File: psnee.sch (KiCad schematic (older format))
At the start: 3 parts, among them IC1 ATTINY45, P1 CONN_ICSP

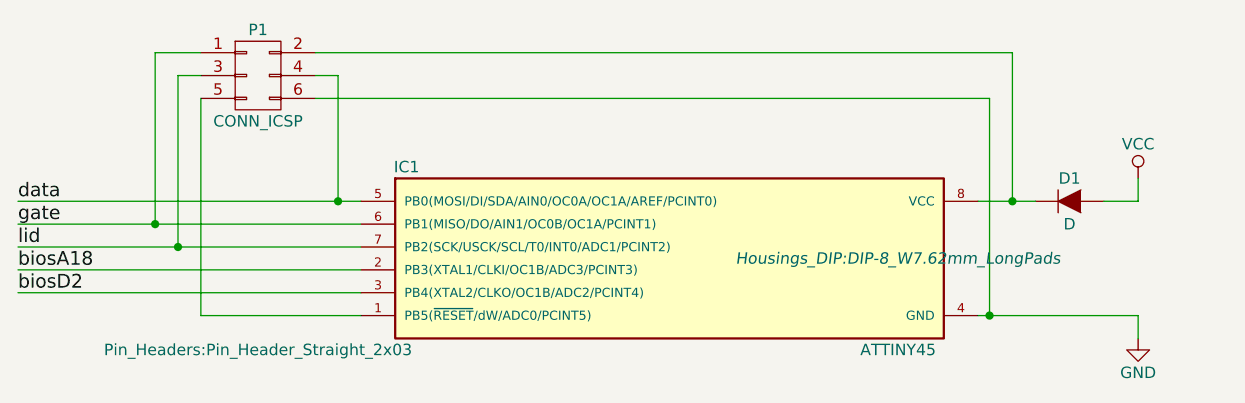
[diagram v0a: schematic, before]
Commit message: updated schematic for v2.0
- added decoupling capacitors
- regenerated annotations
- associated footprints to components
- regenerated netlist
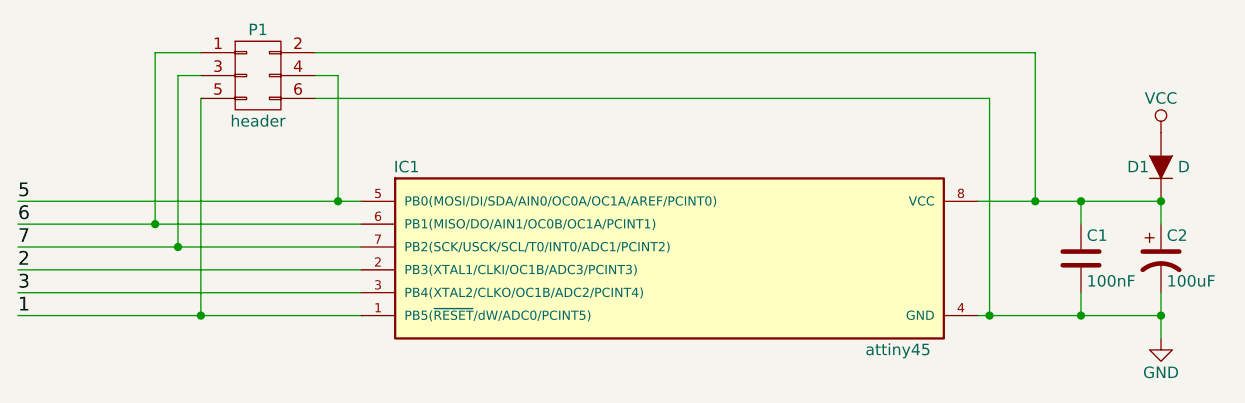
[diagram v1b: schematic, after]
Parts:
- added C1: 100nF, Capacitors_ThroughHole:C_Disc_D6_P5, symbol C
- added C2: 100uF, Capacitors_ThroughHole:C_Radial_D5_L11_P2, symbol CP1
- IC1: value ATTINY45 -> attiny45
- P1: value CONN_ICSP -> header
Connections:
- net GND: now also C1.2, C2.2
- net 1: now reaches IC1.1 (PB5(~RESET~/dW/ADC0/PCINT5)), P1.5 (P5)
- net at D1.1 (K), IC1.8 (VCC), P1.2 (P2): now also C1.1, C2.1
- net biosA18 renamed 2
- net biosD2 renamed 3
- net data renamed 5
- net gate renamed 6
- net lid renamed 7
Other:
- moved on the sheet: D1
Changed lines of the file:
@@
 Sheet 1 1
 Title "PSNee[t]"
-Date "2017-11-02"
-Rev "1.0"
+Date "2018-01-06"
+Rev "2.0"
 Comp ""
 Comment1 ""
@@
 L GND #PWR01
 U 1 1 59F4F857
-P 8050 4000
-F 0 "#PWR01" H 8050 3750 50  0001 C CNN
-F 1 "GND" H 8050 3850 50  0000 C CNN
-F 2 "" H 8050 4000 50  0000 C CNN
-F 3 "" H 8050 4000 50  0000 C CNN
-	1    8050 4000
+P 8150 4000
+F 0 "#PWR01" H 8150 3750 50  0001 C CNN
+F 1 "GND" H 8150 3850 50  0000 C CNN
+F 2 "" H 8150 4000 50  0000 C CNN
+F 3 "" H 8150 4000 50  0000 C CNN
+	1    8150 4000
 	1    0    0    -1
 $EndComp
@@
 P 4200 2850
 F 0 "P1" H 4200 3050 50  0000 C CNN
-F 1 "CONN_ICSP" H 4200 2650 50  0000 C CNN
-F 2 "Pin_Headers:Pin_Header_Straight_2x03" H 4200 1650 50  0000 C CNN
+F 1 "header" H 4200 2650 50  0000 C CNN
+F 2 "Pin_Headers:Pin_Header_Straight_2x03" H 5000 3050 50  0001 C CNN
 F 3 "" H 4200 1650 50  0000 C CNN
 	1    4200 2850
@@
 L D D1
 U 1 1 59F51343
-P 7750 3400
-F 0 "D1" H 7750 3500 50  0000 C CNN
-F 1 "D" H 7750 3300 50  0000 C CNN
-F 2 "Diodes_ThroughHole:Diode_DO-35_SOD27_Horizontal_RM10" H 7750 3400 50  0001 C CNN
-F 3 "" H 7750 3400 50  0000 C CNN
-	1    7750 3400
-	1    0    0    -1
+P 8150 3250
+F 0 "D1" V 8150 3350 50  0000 C CNN
+F 1 "D" V 8150 3150 50  0000 C CNN
+F 2 "Diodes_ThroughHole:Diode_DO-35_SOD27_Horizontal_RM10" H 8150 3250 50  0001 C CNN
+F 3 "" H 8150 3250 50  0000 C CNN
+	1    8150 3250
+	0    -1   -1   0
 $EndComp
 $Comp
 L VCC #PWR02
 U 1 1 59F5217C
-P 8050 3300
-F 0 "#PWR02" H 8050 3150 50  0001 C CNN
-F 1 "VCC" H 8050 3450 50  0000 C CNN
-F 2 "" H 8050 3300 50  0000 C CNN
-F 3 "" H 8050 3300 50  0000 C CNN
-	1    8050 3300
+P 8150 3100
+F 0 "#PWR02" H 8150 2950 50  0001 C CNN
+F 1 "VCC" H 8150 3250 50  0000 C CNN
+F 2 "" H 8150 3100 50  0000 C CNN
+F 3 "" H 8150 3100 50  0000 C CNN
+	1    8150 3100
 	1    0    0    -1
 $EndComp
@@
 P 6000 3650
 F 0 "IC1" H 4850 4050 50  0000 C CNN
-F 1 "ATTINY45" H 7000 3250 50  0000 C CNN
-F 2 "Housings_DIP:DIP-8_W7.62mm_LongPads" H 7000 3650 50  0000 C CIN
+F 1 "attiny45" H 7000 3250 50  0000 C CNN
+F 2 "Housings_DIP:DIP-8_W7.62mm_LongPads" H 6450 4050 50  0001 C CIN
 F 3 "" H 6000 3650 50  0000 C CNN
 	1    6000 3650
 	1    0    0    -1
 $EndComp
-Wire Wire Line
-	7350 3400 7600 3400
-Wire Wire Line
-	7350 3900 8050 3900
+Text Label 3150 3400 0    60   ~ 0
+5
+Text Label 3150 3500 0    60   ~ 0
+6
+Text Label 3150 3600 0    60   ~ 0
+7
+Text Label 3150 3700 0    60   ~ 0
+2
+Text Label 3150 3800 0    60   ~ 0
+3
+Text Label 3150 3900 0    60   ~ 0
+1
+$Comp
+L C C1
+U 1 1 5A5142A1
+P 7800 3650
+F 0 "C1" H 7825 3750 50  0000 L CNN
+F 1 "100nF" H 7825 3550 50  0000 L CNN
+F 2 "Capacitors_ThroughHole:C_Disc_D6_P5" H 7838 3500 50  0001 C CNN
+F 3 "" H 7800 3650 50  0000 C CNN
+	1    7800 3650
+	1    0    0    -1
+$EndComp
+$Comp
+L CP1 C2
+U 1 1 5A5143A7
+P 8150 3650
+F 0 "C2" H 8175 3750 50  0000 L CNN
+F 1 "100uF" H 8175 3550 50  0000 L CNN
+F 2 "Capacitors_ThroughHole:C_Radial_D5_L11_P2" H 8150 3650 50  0001 C CNN
+F 3 "" H 8150 3650 50  0000 C CNN
+	1    8150 3650
+	1    0    0    -1
+$EndComp
 Wire Wire Line
 	3150 3500 4650 3500
@@
 	3950 2950 3950 3900
 Wire Wire Line
-	3950 3900 4650 3900
+	3150 3900 4650 3900
 Wire Wire Line
 	4450 2950 7400 2950
 Wire Wire Line
-	7400 2950 7400 3900
-Connection ~ 7400 3900
-Wire Wire Line
-	4450 2750 7500 2750
-Wire Wire Line
-	7500 2750 7500 3400
-Connection ~ 7500 3400
+	4450 2750 7600 2750
 Wire Wire Line
 	3950 2850 3850 2850
@@
 	4550 2850 4550 3400
 Connection ~ 4550 3400
-Text Label 3150 3400 0    60   ~ 0
-data
-Text Label 3150 3500 0    60   ~ 0
-gate
-Text Label 3150 3600 0    60   ~ 0
-lid
-Text Label 3150 3700 0    60   ~ 0
-biosA18
-Text Label 3150 3800 0    60   ~ 0
-biosD2
 Wire Wire Line
-	8050 3900 8050 4000
+	4650 3800 3150 3800
+Connection ~ 3950 3900
+Wire Wire Line
+	8150 3800 8150 4000
+Connection ~ 8150 3900
+Wire Wire Line
+	7800 3800 7800 3900
+Connection ~ 7800 3900
+Wire Wire Line
+	7350 3900 8150 3900
+Connection ~ 7600 3400
+Wire Wire Line
+	7350 3400 8150 3400
+Wire Wire Line
+	7600 2750 7600 3400
+Wire Wire Line
+	7400 2950 7400 3900
+Connection ~ 7400 3900
+Connection ~ 8150 3400
+Wire Wire Line
+	8150 3400 8150 3500
+Connection ~ 7800 3400
+Wire Wire Line
+	7800 3400 7800 3500
 Wire Wire Line
 	4650 3700 3150 3700
-Wire Wire Line
-	4650 3800 3150 3800
-Wire Wire Line
-	7900 3400 8050 3400
-Wire Wire Line
-	8050 3400 8050 3300
 $EndSCHEMATC
